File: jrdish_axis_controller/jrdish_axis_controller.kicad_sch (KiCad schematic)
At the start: 23 parts, among them J1 Conn_ARM_SWD_TagConnect_TC2030, SW1 DSHP04TSGER, U1 STM32G474RET6, X1 NX2016SA-16MHZ-EXS00A-CS07826

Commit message: Making refinements
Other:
- note added: "PA8,9,10,11 should be configured to internal pull-up."
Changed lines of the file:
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@@
+		)
+	)
+	(text "PA8,9,10,11 should be \nconfigured to internal pull-up."
+		(exclude_from_sim no)
+		(at 131.572 80.264 0)
+		(effects
+			(font
+				(size 1.27 1.27)
+			)
+			(justify left)
 		)
 	)

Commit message: Making refinements
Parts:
- added TP4: RH-5016, MyParts:TESTPOINT-SMD_L3.0-W2.0, symbol MyParts:RH-5016
- U1: Manufacturer ST(意法半导体) -> ST
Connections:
- net 3V3: now also TP4.1
- net GND: no longer C1.2, C10.2, C11.2, C12.2, C13.2, C14.1, C2.2, C3.2, C4.2, C5.2, C6.2, C7.2, C8.2, C9.2, J1.5 (GND), LED1.1 (K), R2.1, SW1.5 (B4), SW1.6 (B3), SW1.7 (B2), SW1.8 (B1), U1.15 (VSS), U1.27 (VSSA), U1.31 (VSS), U1.47 (VSS), U1.63 (VSS), X1.2 (GND), X1.4 (GND)
- new net: C7.2, C8.2
- new net: C14.1, X1.4 (GND)
- new net: C13.2, X1.2 (GND)
- new net: C1.2, C2.2, C3.2, C4.2, C5.2, C6.2
- new net: C10.2, C9.2
- new net: U1.15 (VSS), U1.27 (VSSA), U1.31 (VSS), U1.47 (VSS), U1.63 (VSS)
- new net: SW1.5 (B4), SW1.6 (B3), SW1.7 (B2), SW1.8 (B1)
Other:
- note added: "Test point in upper right area of board"
- title: MCU/Overview -> Dual Axis Controller
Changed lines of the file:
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@@
 	(paper "A4")
 	(title_block
-		(title "MCU/Overview")
-		(date "2026-04-12")
+		(title "Dual Axis Controller")
+		(date "2026-04-30")
 		(rev "1.0")
 		(company "JRSeti")
@@
 		)
 	)
+	(text "Test point in upper right\narea of board"
+		(exclude_from_sim no)
+		(at 106.934 139.446 0)
+		(effects
+			(font
+				(size 1.27 1.27)
+			)
+		)
+	)
 	(text "Dual Axis Controller"
 		(exclude_from_sim no)
@@
 	(wire
 		(pts
+			(xy 100.33 133.35) (xy 101.6 133.35)
+		)
+		(stroke
+			(width 0)
+			(type default)
+		)
+	)
+	(wire
+		(pts
 			(xy 104.14 92.71) (xy 125.73 92.71)
 		)
@@
 		)
 	)
+	(global_label "3V3"
+		(shape input)
+		(at 100.33 133.35 180)
+		(fields_autoplaced yes)
+		(effects
+			(font
+				(size 1.27 1.27)
+			)
+			(justify right)
+		)
+		(property "Intersheetrefs" "${INTERSHEET_REFS}"
+			(at 93.2324 133.35 0)
+			(hide yes)
+			(show_name no)
+			(do_not_autoplace no)
+			(effects
+				(font
+					(size 1.27 1.27)
+				)
+				(justify right)
+			)
+		)
+	)
 	(global_label "SCL_MCU"
 		(shape input)
@@
 	)
 	(symbol
+		(lib_id "MyParts:RH-5016")
+		(at 105.41 133.35 0)
+		(unit 1)
+		(body_style 1)
+		(exclude_from_sim no)
+		(in_bom yes)
+		(on_board yes)
+		(in_pos_files yes)
+		(dnp no)
+		(fields_autoplaced yes)
+		(property "Reference" "TP4"
+			(at 110.49 132.0799 0)
+			(show_name no)
+			(do_not_autoplace no)
+			(effects
+				(font
+					(size 1.27 1.27)
+				)
+				(justify left)
+			)
+		)
+		(property "Value" "RH-5016"
+			(at 110.49 134.6199 0)
+			(show_name no)
+			(do_not_autoplace no)
+			(effects
+				(font
+					(size 1.27 1.27)
+				)
+				(justify left)
+			)
+		)
+		(property "Footprint" "MyParts:TESTPOINT-SMD_L3.0-W2.0"
+			(at 105.41 140.97 0)
+			(hide yes)
+			(show_name no)
+			(do_not_autoplace no)
+			(effects
+				(font
+					(size 1.27 1.27)
+				)
+			)
+		)
+		(property "Datasheet" "https://www.lcsc.com/datasheet/C5199799.pdf"
+			(at 105.41 143.51 0)
+			(hide yes)
+			(show_name no)
+			(do_not_autoplace no)
+			(effects
+				(font
+					(size 1.27 1.27)
+				)
+			)
+		)
+		(property "Description" ""
+			(at 105.41 133.35 0)
+			(hide yes)
+			(show_name no)
+			(do_not_autoplace no)
+			(effects
+				(font
+					(size 1.27 1.27)
+				)
+			)
+		)
+		(property "Manufacturer" "荣和"
+			(at 105.41 146.05 0)
+			(hide yes)
+			(show_name no)
+			(do_not_autoplace no)
+			(effects
+				(font
+					(size 1.27 1.27)
+				)
+			)
+		)
+		(property "MPN" "RH-5016"
+			(at 105.41 148.59 0)
+			(hide yes)
+			(show_name no)
+			(do_not_autoplace no)
+			(effects
+				(font
+					(size 1.27 1.27)
+				)
+			)
+		)
+		(property "LCSC Part" "C5199799"
+			(at 105.41 151.13 0)
+			(hide yes)
+			(show_name no)
+			(do_not_autoplace no)
+			(effects
+				(font
+					(size 1.27 1.27)
+				)
+			)
+		)
+		(pin "1"
+		)
+		(instances
+			(project "jrdish_axis_controller"
+				(path "/10d7c3e5-be4d-4306-a59e-500b86bd141f"
+					(reference "TP4")
+					(unit 1)
+				)
+			)
+		)
+	)
+	(symbol
 		(lib_id "PCM_JLCPCB-Capacitors:0402,100nF")
 		(at 67.31 25.4 0)
@@
 			)
 		)
-		(property "Datasheet" "https://lcsc.com/product-detail/No-specification-for-star-making-plan_STMicroelectronics-STM32G474RET6_C521608.html"
+		(property "Datasheet" "https://www.lcsc.com/datasheet/C521608.pdf?spm=wm.sxq.inf.ggs&lcsc_vid=FFBaV1wHQFldUVICFgBfBVJTQVJWXgBfEQRYBAFQE1YxVlNRQFdeU11fQVRWXztW"
 			(at 80.01 130.81 0)
 			(hide yes)
@@
 			)
 		)
-		(property "Manufacturer" "ST(意法半导体)"
+		(property "Manufacturer" "ST"
 			(at 80.01 133.35 0)
 			(hide yes)

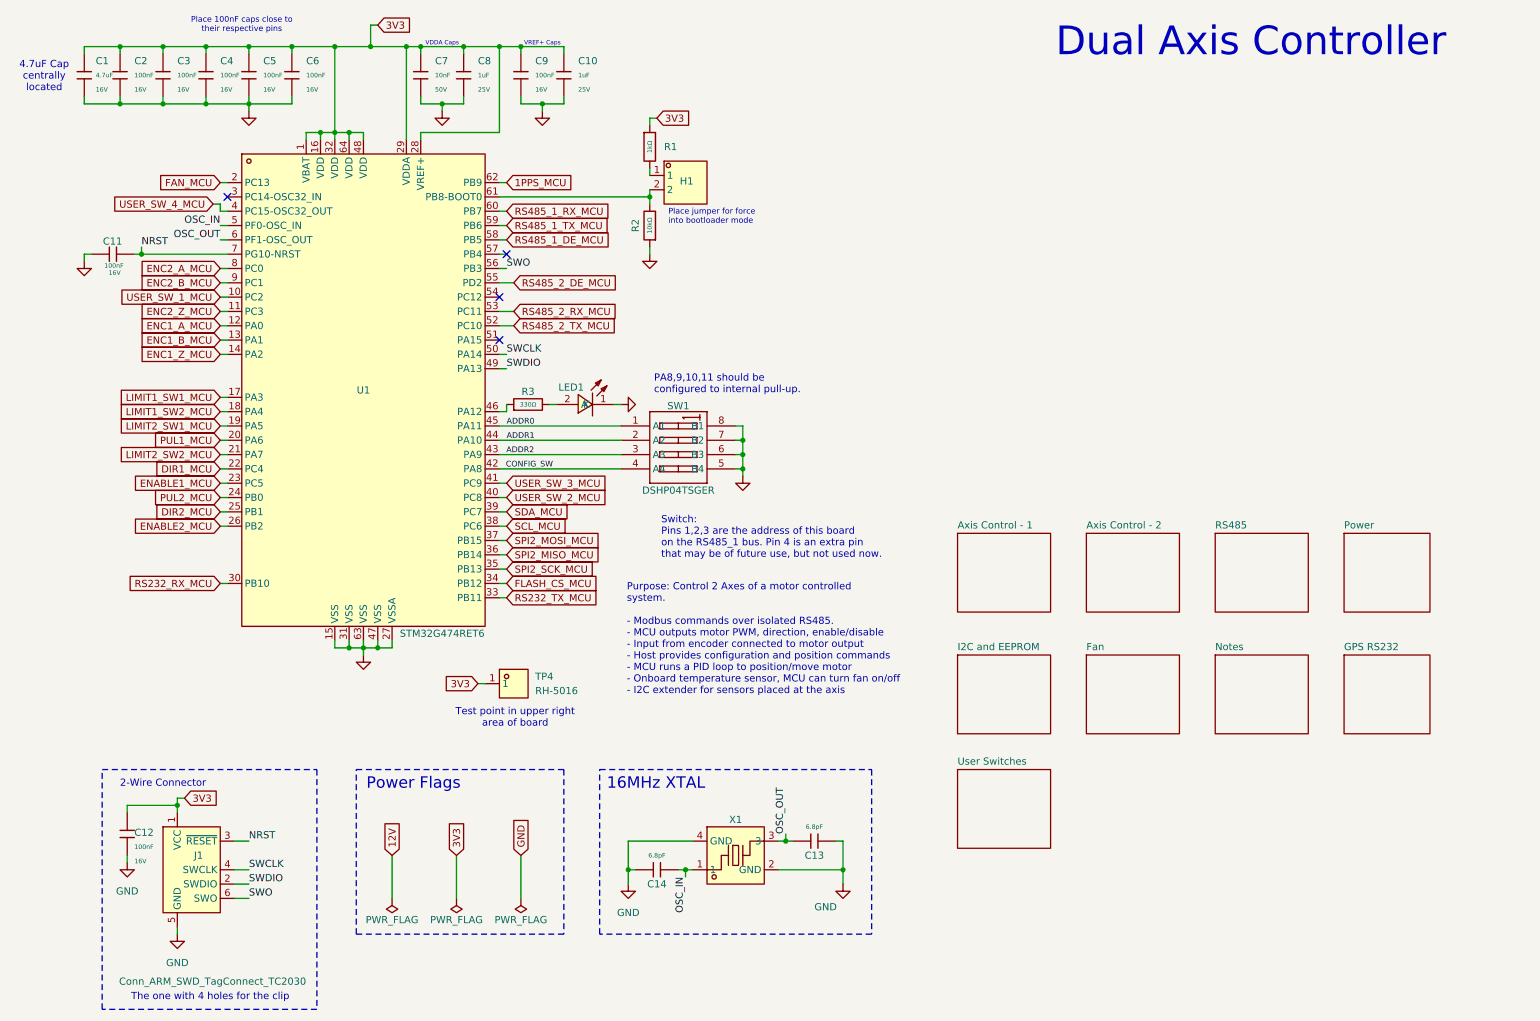
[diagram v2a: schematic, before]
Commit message: Limit switches with mosfets
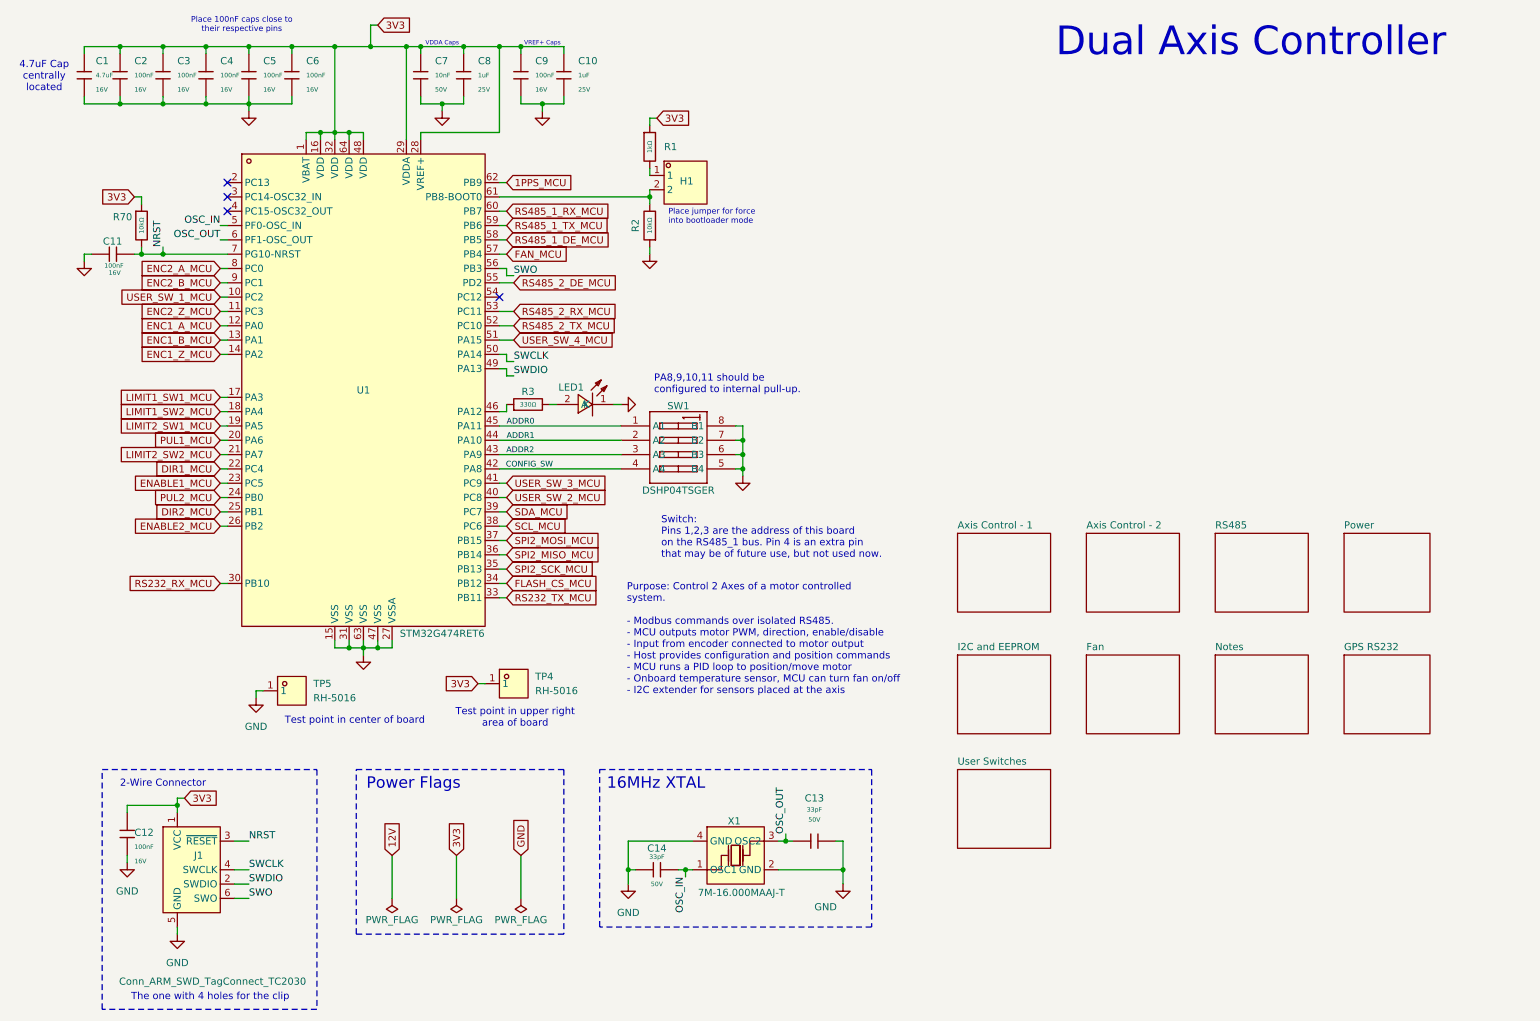
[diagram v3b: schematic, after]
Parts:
- removed C13, C14: 6.8pF, PCM_JLCPCB:C_0402, symbol PCM_JLCPCB-Capacitors:0402,6.8pF
- removed X1: NX2016SA-16MHZ-EXS00A-CS07826, MyParts:CRYSTAL-SMD_4P-L2.0-W1.6-BL, symbol MyParts:NX2016SA-16MHZ-EXS00A-CS07826
- added C13, C14: 33pF, PCM_JLCPCB:C_0402, symbol PCM_JLCPCB-Capacitors:0402,33pF
- added R70: 10kΩ, PCM_JLCPCB:R_0402, symbol PCM_JLCPCB-Resistors:0402,10kΩ
- added TP5: RH-5016, MyParts:TESTPOINT-SMD_L3.0-W2.0, symbol MyParts:RH-5016
- added X1: 7M-16.000MAAJ-T, MyParts:OSC-SMD_4P-L3.2-W2.5-BL-OXETDLJANF-0.032768MHZ, symbol MyParts:7M-16.000MAAJ-T
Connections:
- net 3V3: now also R70.1
- net FAN_MCU: now also U1.57 (PB4); no longer U1.2 (PC13)
- net GND: now also C1.2, C10.2, C11.2, C12.2, C2.2, C3.2, C4.2, C5.2, C6.2, C7.2, C8.2, C9.2, J1.5 (GND), LED1.1 (K), R2.1, SW1.5 (B4), SW1.6 (B3), SW1.7 (B2), SW1.8 (B1), U1.15 (VSS), U1.27 (VSSA), U1.31 (VSS), U1.47 (VSS), U1.63 (VSS), C13.2, C14.1, TP5.1, X1.2 (GND), X1.4 (GND)
- net NRST: now also R70.2
- net OSC_IN: now also C14.2, X1.1 (OSC1)
- net OSC_OUT: now also C13.1, X1.3 (OSC2)
- net USER_SW_4_MCU: now also U1.51 (PA15); no longer U1.4 (PC15-OSC32_OUT)
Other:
- note added: "Test point in center of board"

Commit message: Refinements...
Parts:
- removed H1: 210S-1*2P L=11.6MMGold-plated black, MyParts:HDR-TH_2P-P2.54-V-M-1, symbol MyParts:210S-1*2PL=11.6MMGold-platedblack
- removed R1: 1kΩ, PCM_JLCPCB:R_0402, symbol PCM_JLCPCB-Resistors:0402,1kΩ
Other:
- note added: "Purpose: Control 2 Axes of a motor controlled system. - Modbus commands over isolated RS485. - MCU outputs motor PWM, direction, enable/disable - Input from encoder connected to motor output - Host provides configuration and position commands - MCU runs a PID loop to position/move motor - Onboard temperature sensor, MCU can turn fan on/off - I2C extender for sensors placed at the axis - 3V3 UART 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"
- note removed: "Place jumper for force into bootloader mode"
- note removed: "Purpose: Control 2 Axes of a motor controlled system. - Modbus commands over isolated RS485. - MCU outputs motor PWM, direction, enable/disable - Input from encoder connected to motor output - Host provides configuration and position commands - MCU runs a PID loop to position/move motor - Onboard temperature sensor, MCU can turn fan on/off - I2C extender for sensors placed at the axis"

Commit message: Minor adjustments
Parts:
- removed C13, C14: 33pF, PCM_JLCPCB:C_0402, symbol PCM_JLCPCB-Capacitors:0402,33pF
- removed X1: 7M-16.000MAAJ-T, MyParts:OSC-SMD_4P-L3.2-W2.5-BL-OXETDLJANF-0.032768MHZ, symbol MyParts:7M-16.000MAAJ-T
- added C13, C14: 6.8pF, PCM_JLCPCB:C_0402, symbol PCM_JLCPCB-Capacitors:0402,6.8pF
- added X1: NX2016SA-16MHZ-EXS00A-CS07826, MyParts:CRYSTAL-SMD_4P-L2.0-W1.6-BL, symbol MyParts:NX2016SA-16MHZ-EXS00A-CS07826
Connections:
- net GND: now also C13.2, C14.1, X1.2 (GND), X1.4 (GND)
- net OSC_IN: now also C14.2, X1.1
- net OSC_OUT: now also C13.1, X1.3
